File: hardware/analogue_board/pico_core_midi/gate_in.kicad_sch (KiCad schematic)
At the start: 31 parts, among them J810 Holes, left top, J811 Holes, left bottom, J812 Holes, right top, J813 Holes, right middle, U801 LM393DR2G, U802 LM393DR2G

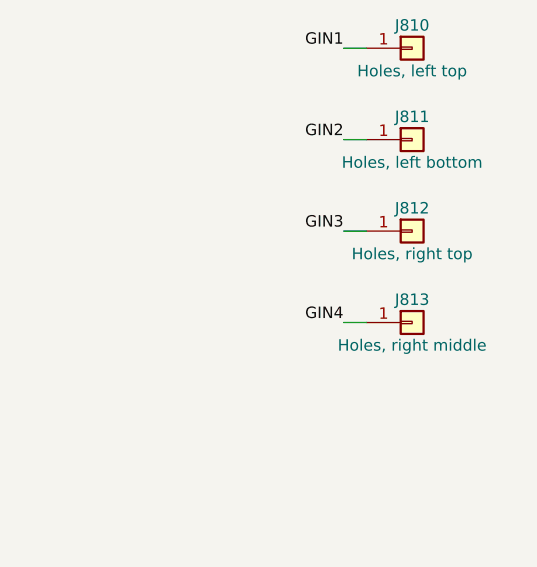
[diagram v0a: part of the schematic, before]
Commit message: Analogue board: the Pico board routes completely
pico_core_midi (Pico 2 / ESP32-P4, the core set with MIDI) routes with no unconnected item
and no copper fault, and every IC supply pin within 4 mm of its capacitor. Routed board in
pico_core_midi/routed_trial/, labels and wiring map, JLC files in pico_core_midi/fab/. Held:
David orders it after the Teensy board's bring-up.

What got it there:
- David's re-laid top: no chip over another on the opposite face (ADC lowered, DAC and CV
  op-amp turned and stacked, DG412s and U504 where nothing is above them, U203 moved out);
  the right-top wiring bank into the right strip's gap; no bus test points; U204 out from
  under the module
- autoroute.py --plane=+5VD: a +5VD plane on In4 whose pads get their own vias before routing
  (stage 1 left 14 instead of 35)
- finish.py: escape lanes kept clear of pre-route ground vias (ADC pin 2 had been fenced in by
  six); decoupling tracks protected from rip-up; plane nets handled throughout
- finish.py fixes: an empty route that looped for hours (no empty routes, a no-progress
  guard); row-at-a-time marking and A* search; KiCad's own dead ends removed

Journal, README and spec updated with the result.

Co-Authored-By: Claude Opus 5.5 <noreply@anthropic.com>
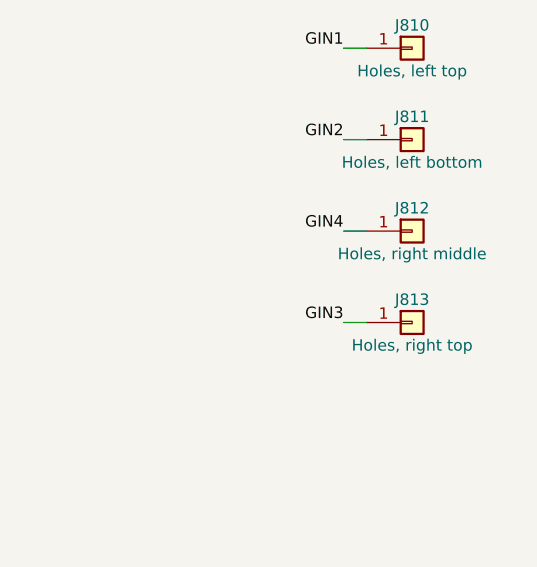
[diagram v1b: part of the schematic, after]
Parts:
- J812: value Holes, right top -> Holes, right middle
- J813: value Holes, right middle -> Holes, right top
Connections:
- net GIN3: now also J813.1 (Pin_1); no longer J812.1 (Pin_1)
- net GIN4: now also J812.1 (Pin_1); no longer J813.1 (Pin_1)
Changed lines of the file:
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@@
 			)
 		)
-		(property "Value" "Holes, right top"
+		(property "Value" "Holes, right middle"
 			(at 330.2 76.2 0)
 			(effects
@@
 		)
 	)
-	(label "GIN3"
+	(label "GIN4"
 		(at 322.58 73.66 180)
 		(effects
@@
 			)
 		)
-		(property "Value" "Holes, right middle"
+		(property "Value" "Holes, right top"
 			(at 330.2 86.36 0)
 			(effects
@@
 		)
 	)
-	(label "GIN4"
+	(label "GIN3"
 		(at 322.58 83.82 180)
 		(effects
